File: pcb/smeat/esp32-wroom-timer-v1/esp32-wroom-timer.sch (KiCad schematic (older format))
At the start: 61 parts, among them J1 Fan_connector, J2 Programming, J3 input power, J4 Conn_Coaxial, Q1 Q_NMOS_GSD, Q2 Q_NMOS_GSD, U1 ESP32-WROOM-32U, U10 RX5808, U11 RX5808, U12 MCP9804_MSOP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

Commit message: Possibly the final version(?)
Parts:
- D2: footprint Diode_SMD:D_SOD-123 -> Diode_SMD:D_SMA
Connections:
- net ADC5: now also R6.1, R7.2
- net ADC6: no longer R6.1, R7.2
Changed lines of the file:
@@
 Text Label 3500 4100 2    50   ~ 0
 ADC4
-Text Label 1700 2000 0    50   ~ 0
-ADC5
 $Comp
 L power:GND #PWR02
@@
 	3200 5550 3300 5550
 Text Label 3300 5950 1    50   ~ 0
-ADC6
+ADC5
 Wire Wire Line
 	3300 5950 3300 5550
@@
 F 0 "D2" H 2450 6834 50  0000 C CNN
 F 1 "D" H 2450 6925 50  0000 C CNN
-F 2 "Diode_SMD:D_SOD-123" H 2450 7050 50  0001 C CNN
+F 2 "Diode_SMD:D_SMA" H 2450 7050 50  0001 C CNN
 F 3 "~" H 2450 7050 50  0001 C CNN
 	1    2450 7050
@@
 	-1   0    0    1
 $EndComp
-Text Label 1700 2100 0    50   ~ 0
-ADC6
 Wire Wire Line
 	3100 3800 3500 3800
@@
 Wire Wire Line
 	10900 3850 10600 3850
-Text Label 10900 3750 2    50   ~ 0
-ADC6
 Wire Wire Line
 	10900 3750 10600 3750
@@
 	1    0    0    -1
 $EndComp
+Text Label 10900 3750 2    50   ~ 0
+ADC6
+Text Label 1700 2100 0    50   ~ 0
+ADC6
+Text Label 1700 2000 0    50   ~ 0
+ADC5
 $EndSCHEMATC

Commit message: Add safety pullup resistors for i2c
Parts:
- added R18, R19: 4K7, Resistor_SMD:R_0805_2012Metric, symbol Device:R
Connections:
- net +3V3: now also R18.1, R19.1
- net SCL: now also R18.2
- net SDA: now also R19.2
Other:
- note added: "Safety pullups for I2C\nProbably unpopulated"
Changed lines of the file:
@@
 Text Label 1700 2000 0    50   ~ 0
 ADC5
+$Comp
+L Device:R R19
+U 1 1 5D5C2BE1
+P 4400 4150
+F 0 "R19" H 4330 4104 50  0000 R CNN
+F 1 "4K7" V 4400 4200 50  0000 R CNN
+F 2 "Resistor_SMD:R_0805_2012Metric" V 4330 4150 50  0001 C CNN
+F 3 "~" H 4400 4150 50  0001 C CNN
+	1    4400 4150
+	0    1    1    0
+$EndComp
+$Comp
+L Device:R R18
+U 1 1 5D5C3405
+P 4400 3850
+F 0 "R18" H 4330 3804 50  0000 R CNN
+F 1 "4K7" V 4400 3900 50  0000 R CNN
+F 2 "Resistor_SMD:R_0805_2012Metric" V 4330 3850 50  0001 C CNN
+F 3 "~" H 4400 3850 50  0001 C CNN
+	1    4400 3850
+	0    1    1    0
+$EndComp
+Text Label 4050 4150 0    50   ~ 0
+SDA
+Text Label 4050 3850 0    50   ~ 0
+SCL
+Wire Wire Line
+	4050 3850 4250 3850
+Wire Wire Line
+	4050 4150 4250 4150
+$Comp
+L power:+3.3V #PWR015
+U 1 1 5D5F5D25
+P 4800 4000
+F 0 "#PWR015" H 4800 3850 50  0001 C CNN
+F 1 "+3.3V" H 4815 4173 50  0000 C CNN
+F 2 "" H 4800 4000 50  0001 C CNN
+F 3 "" H 4800 4000 50  0001 C CNN
+	1    4800 4000
+	0    1    1    0
+$EndComp
+Wire Wire Line
+	4550 3850 4800 3850
+Wire Wire Line
+	4800 3850 4800 4000
+Wire Wire Line
+	4550 4150 4800 4150
+Wire Wire Line
+	4800 4150 4800 4000
+Connection ~ 4800 4000
+Text Notes 4050 3600 0    50   ~ 0
+Safety pullups for I2C\nProbably unpopulated
 $EndSCHEMATC

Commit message: Last minute PCB changes I hate those :/
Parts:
- added C14, C15: 0.1µF, Capacitor_SMD:C_0603_1608Metric, symbol Device:C
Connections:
- net +3V3: now also C14.1, C15.1
- net ADC3: now also U1.7 (IO35); no longer U1.6 (IO34)
- net ADC4: now also U1.6 (IO34); no longer U1.7 (IO35)
- net GND: now also C14.2, C15.2
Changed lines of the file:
@@
 Wire Wire Line
 	1700 2100 1900 2100
+Text Label 3500 4100 2    50   ~ 0
+ADC3
 Text Label 3500 4000 2    50   ~ 0
-ADC3
-Text Label 3500 4100 2    50   ~ 0
 ADC4
 $Comp
@@
 	1    0    0    -1
 $EndComp
-$Comp
-L power:+28V #PWR0112
-U 1 1 5D4CF0E1
-P 5550 7450
-F 0 "#PWR0112" H 5550 7300 50  0001 C CNN
-F 1 "+28V" V 5565 7578 50  0000 L CNN
-F 2 "" H 5800 7500 50  0001 C CNN
-F 3 "" H 5800 7500 50  0001 C CNN
-	1    5550 7450
-	-1   0    0    1
-$EndComp
-$Comp
-L power:+BATT #PWR0113
-U 1 1 5D4DE0AD
-P 5550 6950
-F 0 "#PWR0113" H 5550 6800 50  0001 C CNN
-F 1 "+BATT" V 5565 7077 50  0000 L CNN
-F 2 "" H 5550 6950 50  0001 C CNN
-F 3 "" H 5550 6950 50  0001 C CNN
-	1    5550 6950
-	1    0    0    -1
-$EndComp
-Wire Wire Line
-	5700 7150 6050 7150
 Wire Wire Line
 	5550 7450 5550 7350
@@
 $EndComp
 Wire Wire Line
-	5950 7250 6050 7250
+	5950 7250 6000 7250
 $Comp
 L power:+3.3V #PWR0136
 U 1 1 5D56B678
-P 6000 7400
-F 0 "#PWR0136" H 6000 7250 50  0001 C CNN
-F 1 "+3.3V" V 6015 7528 50  0000 L CNN
-F 2 "" H 6000 7400 50  0001 C CNN
-F 3 "" H 6000 7400 50  0001 C CNN
-	1    6000 7400
-	-1   0    0    1
+P 5950 7750
+F 0 "#PWR0136" H 5950 7600 50  0001 C CNN
+F 1 "+3.3V" V 5965 7878 50  0000 L CNN
+F 2 "" H 5950 7750 50  0001 C CNN
+F 3 "" H 5950 7750 50  0001 C CNN
+	1    5950 7750
+	0    -1   -1   0
 $EndComp
 Wire Wire Line
@@
 $EndComp
 Wire Wire Line
-	5550 7050 6050 7050
-Wire Wire Line
 	5700 7350 5550 7350
 Wire Wire Line
@@
 	4450 7100 4250 7100
 Wire Wire Line
-	3850 7400 3850 7500
+	3850 7400 3850 7450
 NoConn ~ 3450 6900
 Wire Wire Line
@@
 Text Notes 6100 3400 0    50   ~ 0
 Footprints are here just in case. \nProbably not populated
-Text Notes 3300 7550 0    50   ~ 0
+Text Notes 3150 7650 0    50   ~ 0
 Optional temperature sensor for fan output
 Text Notes 700  7100 0    50   ~ 0
@@
 Text Notes 5800 6650 0    50   ~ 0
 Current and voltage sense
-Wire Wire Line
-	6000 7400 6000 7350
 Wire Wire Line
 	8050 5450 8050 5500
@@
 Text Notes 4050 3600 0    50   ~ 0
 Safety pullups for I2C\nProbably unpopulated
+$Comp
+L power:+28V #PWR0112
+U 1 1 5D4CF0E1
+P 5550 7450
+F 0 "#PWR0112" H 5550 7300 50  0001 C CNN
+F 1 "+28V" V 5565 7578 50  0000 L CNN
+F 2 "" H 5800 7500 50  0001 C CNN
+F 3 "" H 5800 7500 50  0001 C CNN
+	1    5550 7450
+	-1   0    0    1
+$EndComp
+$Comp
+L power:+BATT #PWR0113
+U 1 1 5D4DE0AD
+P 5550 6950
+F 0 "#PWR0113" H 5550 6800 50  0001 C CNN
+F 1 "+BATT" V 5565 7077 50  0000 L CNN
+F 2 "" H 5550 6950 50  0001 C CNN
+F 3 "" H 5550 6950 50  0001 C CNN
+	1    5550 6950
+	1    0    0    -1
+$EndComp
+Wire Wire Line
+	5700 7150 6050 7150
+Wire Wire Line
+	5550 7050 6050 7050
+$Comp
+L Device:C C14
+U 1 1 5D6BD659
+P 5850 7450
+F 0 "C14" V 5800 7350 50  0000 C CNN
+F 1 "0.1µF" V 5950 7550 50  0000 C CNN
+F 2 "Capacitor_SMD:C_0603_1608Metric" H 5888 7300 50  0001 C CNN
+F 3 "~" H 5850 7450 50  0001 C CNN
+	1    5850 7450
+	-1   0    0    1
+$EndComp
+Wire Wire Line
+	6000 7750 5950 7750
+Wire Wire Line
+	6000 7350 6000 7600
+Wire Wire Line
+	5850 7600 6000 7600
+Connection ~ 6000 7600
+Wire Wire Line
+	6000 7600 6000 7750
+Wire Wire Line
+	5850 7300 6000 7300
+Wire Wire Line
+	6000 7300 6000 7250
+Connection ~ 6000 7250
+Wire Wire Line
+	6000 7250 6050 7250
+$Comp
+L Device:C C15
+U 1 1 5D6FAB65
+P 4100 7450
+F 0 "C15" V 4050 7350 50  0000 C CNN
+F 1 "0.1µF" V 4200 7550 50  0000 C CNN
+F 2 "Capacitor_SMD:C_0603_1608Metric" H 4138 7300 50  0001 C CNN
+F 3 "~" H 4100 7450 50  0001 C CNN
+	1    4100 7450
+	0    -1   -1   0
+$EndComp
+Wire Wire Line
+	3850 7450 3950 7450
+Connection ~ 3850 7450
+Wire Wire Line
+	3850 7450 3850 7500
+$Comp
+L power:GND #PWR016
+U 1 1 5D70E7CA
+P 4250 7450
+F 0 "#PWR016" H 4250 7200 50  0001 C CNN
+F 1 "GND" H 4255 7277 50  0000 C CNN
+F 2 "" H 4250 7450 50  0001 C CNN
+F 3 "" H 4250 7450 50  0001 C CNN
+	1    4250 7450
+	0    -1   -1   0
+$EndComp
 $EndSCHEMATC

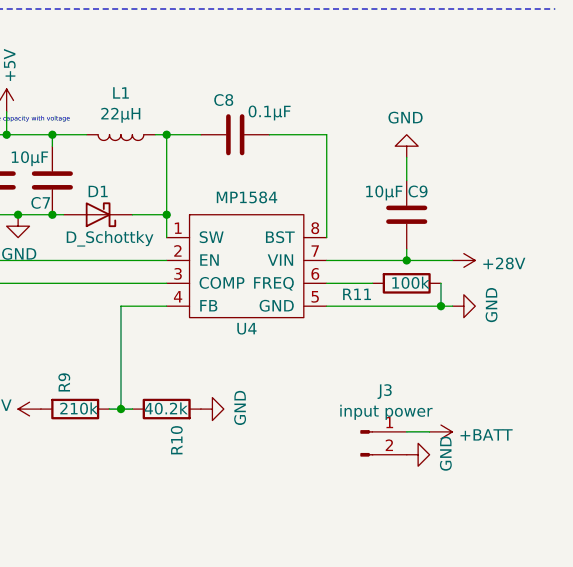
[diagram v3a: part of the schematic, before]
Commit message: [PCB] Fix resistor value
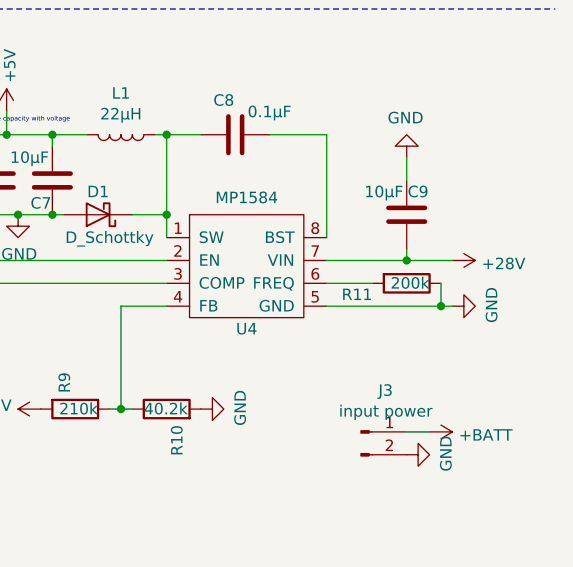
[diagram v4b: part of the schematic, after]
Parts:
- R11: value 100k -> 200k
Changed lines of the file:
@@
 P 10600 5600
 F 0 "R11" V 10650 5450 50  0000 R CNN
-F 1 "100k" V 10600 5700 50  0000 R CNN
+F 1 "200k" V 10600 5700 50  0000 R CNN
 F 2 "Resistor_SMD:R_0805_2012Metric" V 10530 5600 50  0001 C CNN
 F 3 "~" H 10600 5600 50  0001 C CNN
